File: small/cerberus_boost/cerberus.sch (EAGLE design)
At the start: 31 parts, among them Q1 2N5088, Q2 2N5088, Q3 2N5087

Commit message: updates to a few small pedals
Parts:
- removed BOOST: 10kA, potentiometers:POTSSMALL_PADS
- added LEVEL: 10kA, potentiometers:POTSSMALL_PADS
- C1: value 100uF -> 100u
- C2: value .047uF -> 47n
- C3, C7: value 4.7uF -> 4u7
- C4: value .01uF -> 10n
- C5, C6: value 10pF -> 10p
- D1: value 1n5817 -> 1N5817
- R1: value 2M2 -> 1M
- R10: value 8k2 -> 47R
- R11: value 47R -> 8k2
- R13: value 2M2 -> 2M2***
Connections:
- removed net N$11: R6.2, RANGE_A.2
- new net N$8: R6.1, RANGE_A.2
- net +9V: now also PAD1.P$1; no longer PAD2.P$1
- net GND: now also LEVEL.1, R11.1, R3.1; no longer BOOST.1, R10.1, R2.1
- net IN: now also PAD2.P$1; no longer PAD1.P$1
- net N$1: now also R2.1, R3.2; no longer R2.2, R3.1
- net N$10: now also R9.1; no longer R9.2
- net N$12: now also R6.2, R8.1; no longer R6.1, R8.2
- net N$14: now also R8.2; no longer R8.1
- net N$2: now also R10.1; no longer R11.1
- net N$3: now also LEVEL.3; no longer BOOST.3
- net N$6: now also R11.2, R9.2; no longer R10.2, R9.1
- net N$7: now also R10.2, R2.2; no longer R11.2, R3.2
- net OUT: now also LEVEL.2; no longer BOOST.2
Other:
- moved on the sheet: C1, C4, C5, R1, R10, R11, R13, R2, R3, R6, R8, R9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

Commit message: formatting updates
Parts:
- removed LEVEL: 10kA, potentiometers:POTSSMALL_PADS
- C1: value 100u -> 47n; device capacitors-elec:0501 -> capacitors-film:CER/FILMBOX.1
- C2: value 47n -> 100u; device capacitors-film:CER/FILMBOX.1 -> capacitors-elec:0501
- C5, C6: device capacitors-film:CER/FILMBOX.1 -> capacitors-film:CER/FILM2
- RANGE: device switches:DPDT -> switches:DPDTPADS
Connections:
- removed net N$3: C7.-, LEVEL.3, R13.2
- net GND: now also C2.-; no longer C1.-, LEVEL.1
- net IN: now also C1.2; no longer C2.2
- net N$1: now also C1.1; no longer C2.1
- net N$7: now also C2.+; no longer C1.+
- net OUT: now also C7.-, R13.2; no longer LEVEL.2
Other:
- note added: "CERBERUS"
- note added: "THREE-FREQUENCY BOOSTER based on the dan armstrong red ranger (c) 2016 burr settles"
- note added: "range switch: on/off/on 1: +25db treble x: +13db full 3: +22db bass"
- moved on the sheet: C3, C4, C5, C6, C7, D1, Q1, Q2, Q3, R1, R10, R11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

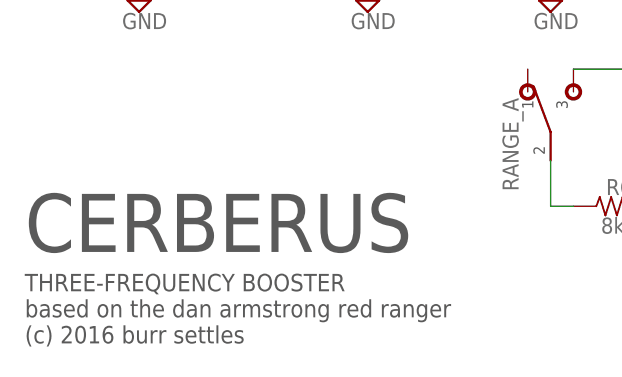
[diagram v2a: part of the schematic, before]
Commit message: add beginnings of tremolo; minor copy tweaks to other schems
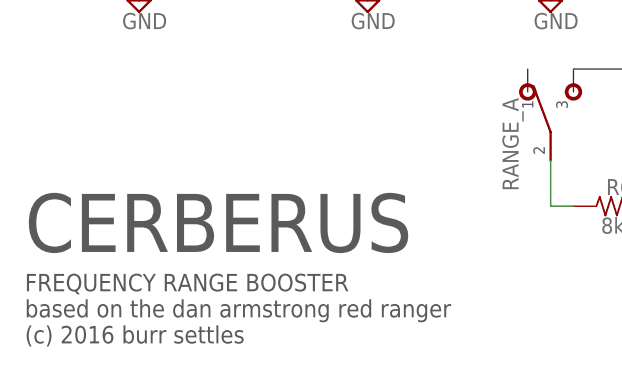
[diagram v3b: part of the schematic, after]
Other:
- note added: "FREQUENCY RANGE BOOSTER based on the dan armstrong red ranger (c) 2016 burr settles"
- note removed: "THREE-FREQUENCY BOOSTER based on the dan armstrong red ranger (c) 2016 burr settles"
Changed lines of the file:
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@@
 <plain>
 <text x="2.54" y="12.7" size="6.4516" layer="97">CERBERUS</text>
-<text x="2.54" y="2.54" size="1.9304" layer="97">THREE-FREQUENCY BOOSTER
+<text x="2.54" y="2.54" size="1.9304" layer="97">FREQUENCY RANGE BOOSTER
 based on the dan armstrong red ranger
 (c) 2016 burr settles</text>
